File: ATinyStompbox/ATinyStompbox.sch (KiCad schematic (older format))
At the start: 56 parts, among them J1 CONN_01X05, J10 6.5mm_JACK_TRS_6PINS, J11 CONN_01X04, J12 Con_JackIN, J13 Con_JackOUT, J14 CONN_01X04, J15 Con_DC, J16 Con_BAT, J17 StompDrillHole, J18 Con_3-5V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

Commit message: small improvements
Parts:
- removed D2: LED, LEDs:LED_D5.0mm_FlatTop, symbol LED
- added D2: LED_Dual_AAC, 8BitMixtape_Stomp:Stomp_LED-Ring_DUAL, symbol LED_Dual_AAC
- D1: footprint LEDs:LED_D5.0mm -> LEDs:LED_PLCC_2835_Handsoldering
- renumbered CV1 to POT1-CV1, Main1 to POT2-Main1, Vol1 to POT3-Vol1
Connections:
- net +9V: now also J16.2 (P2)
- net VCC: now also D2.1 (A1), D2.2 (A2)
- net at SW5.5: now also D2.3 (K)
- net +BATT: no longer names the net of J9.3
- net +BATT: no longer J16.2 (P2)
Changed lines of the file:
@@
 $EndDescr
 $Comp
-L POT Main1
+L POT POT2-Main1
 U 1 1 5B46F160
 P 5200 6150
-F 0 "Main1" V 5025 6150 50  0000 C CNN
+F 0 "POT2-Main1" V 5025 6150 50  0000 C CNN
 F 1 "POT 10K lin Sleeve" V 5100 6150 50  0000 C CNN
 F 2 "8BitMixtape_Stomp:Mixtape_Pot_Alps_RK09L_Sleve_Single_Horizontal" H 5200 6150 50  0001 C CNN
@@
 $EndComp
 $Comp
-L POT CV1
+L POT POT1-CV1
 U 1 1 5B46F2B5
 P 5200 3950
-F 0 "CV1" V 5025 3950 50  0000 C CNN
+F 0 "POT1-CV1" V 5025 3950 50  0000 C CNN
 F 1 "POT 10K lin" V 5100 3950 50  0000 C CNN
 F 2 "8BitMixtapes_all:Mixtape_Pot_Alps_RK09K_Horizontal" H 5200 3950 50  0001 C CNN
@@
 $EndComp
 $Comp
-L POT Vol1
+L POT POT3-Vol1
 U 1 1 5B46F319
 P 7750 3800
-F 0 "Vol1" V 7575 3800 50  0000 C CNN
+F 0 "POT3-Vol1" V 7575 3800 50  0000 C CNN
 F 1 "POT 10k" V 7650 3800 50  0000 C CNN
 F 2 "8BitMixtapes_all:Mixtape_Pot_Alps_RK09K_Horizontal" H 7750 3800 50  0001 C CNN
@@
 Text GLabel 7100 950  0    60   Input ~ 0
 Stomp_from_PCB
-$Comp
-L LED D2
-U 1 1 5B4940CC
-P 8100 1150
-F 0 "D2" H 8100 1250 50  0000 C CNN
-F 1 "LED" H 8100 1050 50  0000 C CNN
-F 2 "LEDs:LED_D5.0mm_FlatTop" H 8100 1150 50  0001 C CNN
-F 3 "" H 8100 1150 50  0001 C CNN
-	1    8100 1150
-	1    0    0    -1
-$EndComp
 $Comp
 L GND #PWR018
@@
 F 0 "D1" H 3000 1450 50  0000 C CNN
 F 1 "LED" H 3000 1250 50  0000 C CNN
-F 2 "LEDs:LED_D5.0mm" H 3000 1350 50  0001 C CNN
+F 2 "LEDs:LED_PLCC_2835_Handsoldering" H 3000 1350 50  0001 C CNN
 F 3 "" H 3000 1350 50  0001 C CNN
 	1    3000 1350
@@
 	7300 3100 7300 3650
 Wire Wire Line
-	7950 1150 7750 1150
-Wire Wire Line
-	8250 1150 8700 1150
-Wire Wire Line
 	6700 1550 7350 1550
 Wire Wire Line
@@
 Wire Wire Line
 	7400 2150 7100 2150
-Text GLabel 7900 950  2    60   Input ~ 0
+Text GLabel 7900 750  2    60   Input ~ 0
 Jack_OUT
 Wire Wire Line
-	7750 950  7900 950
-Wire Wire Line
 	7800 650  7800 950
-Connection ~ 7800 950
 Text GLabel 8350 2200 0    60   Input ~ 0
 Jack_OUT
@@
 Wire Wire Line
 	4600 1650 4700 1650
-Wire Wire Line
-	5000 2300 5100 2300
-Wire Wire Line
-	5100 2300 5100 1550
 Connection ~ 4700 1550
 $Comp
@@
 Wire Wire Line
 	8500 5550 8350 5550
+Wire Wire Line
+	5100 1550 5100 2200
+Connection ~ 5100 2200
+Wire Wire Line
+	7900 750  7800 750
+Connection ~ 7800 750
+Wire Wire Line
+	7800 950  7750 950
+Wire Wire Line
+	7800 1150 7750 1150
+$Comp
+L LED_Dual_AAC D2
+U 1 1 5B523102
+P 8100 1150
+F 0 "D2" H 8100 1375 50  0000 C CNN
+F 1 "LED_Dual_AAC" H 8100 900 50  0000 C CNN
+F 2 "8BitMixtape_Stomp:Stomp_LED-Ring_DUAL" H 8100 1150 50  0001 C CNN
+F 3 "" H 8100 1150 50  0001 C CNN
+	1    8100 1150
+	1    0    0    -1
+$EndComp
+Wire Wire Line
+	8700 1150 8550 1150
+Wire Wire Line
+	8550 1050 8550 1250
+Wire Wire Line
+	8550 1250 8400 1250
+Wire Wire Line
+	8400 1050 8550 1050
+Connection ~ 8550 1150
 $EndSCHEMATC

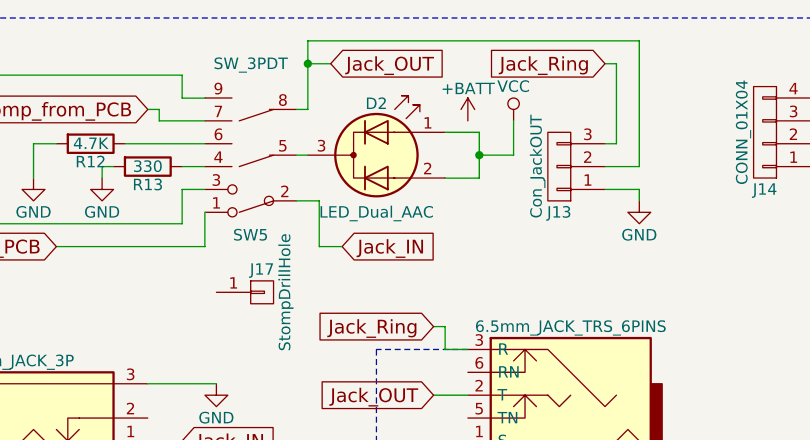
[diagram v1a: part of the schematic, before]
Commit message: new schematics for DualLED
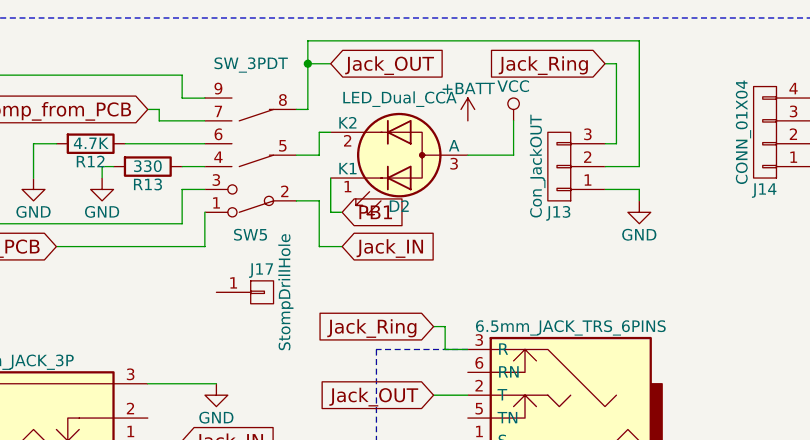
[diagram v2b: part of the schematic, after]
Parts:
- removed D2: LED_Dual_AAC, 8BitMixtape_Stomp:Stomp_LED-Ring_DUAL, symbol LED_Dual_AAC
- added D2: LED_Dual_CCA, symbol LED_Dual_CCA
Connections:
- net PB1: now also D2.1 (K1)
- net VCC: now also D2.3 (A)
- net at SW5.5: now also D2.2 (K2)
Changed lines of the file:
@@
 	7800 950  7750 950
 Wire Wire Line
-	7800 1150 7750 1150
+	7750 1150 7850 1150
+Wire Wire Line
+	8500 1150 8700 1150
 $Comp
-L LED_Dual_AAC D2
-U 1 1 5B523102
-P 8100 1150
-F 0 "D2" H 8100 1375 50  0000 C CNN
-F 1 "LED_Dual_AAC" H 8100 900 50  0000 C CNN
-F 2 "8BitMixtape_Stomp:Stomp_LED-Ring_DUAL" H 8100 1150 50  0001 C CNN
-F 3 "" H 8100 1150 50  0001 C CNN
-	1    8100 1150
-	1    0    0    -1
+L LED_Dual_CCA D2
+U 1 1 5B59A765
+P 8200 1150
+F 0 "D2" H 8200 1375 50  0000 C CNN
+F 1 "LED_Dual_CCA" H 8200 900 50  0000 C CNN
+F 2 "" H 8250 1150 50  0001 C CNN
+F 3 "" H 8250 1150 50  0001 C CNN
+	1    8200 1150
+	-1   0    0    1
 $EndComp
 Wire Wire Line
-	8700 1150 8550 1150
+	7900 1050 7850 1050
 Wire Wire Line
-	8550 1050 8550 1250
+	7850 1050 7850 1150
+Text GLabel 7950 1400 2    60   Input ~ 0
+PB1
 Wire Wire Line
-	8550 1250 8400 1250
+	7900 1250 7900 1400
 Wire Wire Line
-	8400 1050 8550 1050
-Connection ~ 8550 1150
+	7900 1400 7950 1400
 $EndSCHEMATC
